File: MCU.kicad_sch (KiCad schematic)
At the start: 13 parts, among them U2201 ADG1607xCP, U2202 MSP430FR5969IRGZR, U2203 LP38690SDX-3.3/NOPB, U2204 TCAN4551RGYRQ1

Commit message: added second AMUX and housekeeping
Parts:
- added C1903: C_Small, Capacitor_SMD:C_0603_1608Metric_Pad1.08x0.95mm_HandSolder, symbol Device:C_Small
- added R1903: R_Small, Resistor_SMD:R_0603_1608Metric_Pad0.98x0.95mm_HandSolder, symbol Device:R_Small
- added TP1901, TP1902, TP1903, TP1904, TP1905, TP1906, TP1907, TP1908, TP1909, TP1910, TP1911: ~, symbol Connector:TestPoint_Small
- added U1902: ADG1607xCP, Package_CSP:LFCSP-32-1EP_5x5mm_P0.5mm_EP3.1x3.1mm, symbol Analog_Switch:ADG1607xCP
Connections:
- net AMEAS_BUS: now also U2201.21 (S5A); no longer U2202.7 (P3.3/A15/C15)
- net AMEAS_SOL_1: now also U1902.6 (S3B); no longer U2202.4 (P3.0/A12/C12)
- net AMEAS_SOL_2: now also U1902.5 (S4B); no longer U2202.5 (P3.1/A13/C13)
- net AMEAS_SOL_3: now also U1902.4 (S5B); no longer U2202.6 (P3.2/A14/C14)
- net AMUX_0: now also U1902.15 (A0)
- net AMUX_1: now also U1902.14 (A1)
- net AMUX_2: now also U1902.10 (A2)
- net AMUX_EN: now also U1902.16 (EN)
- net GND: now also C1903.1, R1903.1, U1902.25 (V_{SS}), U1902.33 (V_{SS}), U1902.9 (GND)
- net MCU_3V3: now also C1903.2, U1902.29 (V_{DD})
- net TMEAS_BATT_1: now also TP1910.1, U1902.19 (S3A); no longer U2202.39 (P2.3/TA0.0/UCA1STE/A6/C10)
- net TMEAS_BATT_2: now also TP1911.1, U1902.20 (S4A); no longer U2202.40 (P2.4/TA1.0/UCA1CLK/A7/C11)
- net TMEAS_SOL_1: now also TP1907.1
- net TMEAS_SOL_2: now also TP1908.1
- net TMEAS_SOL_3: now also TP1909.1
- net VMEAS_BATT_1: now also TP1905.1, U1902.17 (S1A); no longer U2202.3 (P1.2/TA1.1/TA0CLK/COUT/A2/C2)
- net VMEAS_BATT_2: now also TP1906.1, U1902.18 (S2A); no longer U2202.9 (P1.3/TA1.2/UCB0STE/A3/C3)
- net VMEAS_SOL_1: now also TP1902.1, U1902.21 (S5A); no longer U2202.16 (P4.0/A8)
- net VMEAS_SOL_2: now also TP1903.1, U1902.22 (S6A); no longer U2202.17 (P4.1/A9)
- net VMEAS_SOL_3: now also TP1904.1, U1902.23 (S7A); no longer U2202.18 (P4.2/A10)
- net at U2202.22 (TEST/SBWTCK): now also TP1901.1
- net at U2202.23 (~{RST}/NMI/SBWTDIO): now also R1903.2
- new net ADC_3: U1902.27 (DA), U2202.3 (P1.2/TA1.1/TA0CLK/COUT/A2/C2)
- new net ADC_4: U1902.31 (DB), U2202.9 (P1.3/TA1.2/UCB0STE/A3/C3)
- new net PWM_1: U2202.6 (P3.2/A14/C14)
- new net PWM_2: U2202.5 (P3.1/A13/C13)
- new net PWM_3: U2202.4 (P3.0/A12/C12)
- no-connect marks 1 -> 0
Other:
- moved on the sheet: C2201, U2201

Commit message: connected CAN driver, added 3 solar inputs
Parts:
- added C1904, C1905, C1906: C_Small, Capacitor_SMD:C_0603_1608Metric_Pad1.08x0.95mm_HandSolder, symbol Device:C_Small
- added R1904: R_Small, Resistor_SMD:R_0603_1608Metric_Pad0.98x0.95mm_HandSolder, symbol Device:R_Small
- added TP1912, TP1913, TP1914, TP1915, TP1916, TP1917, TP1918, TP1919: ~, symbol Connector:TestPoint_Small
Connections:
- net Ch_O_EN_11: now also TP1918.1
- net Ch_O_EN_12: now also TP1919.1
- net GND: now also U2204.20 (OSC2), C1904.1, C1905.1, C1906.1
- net MCU_3V3: now also U2204.15 (INH), U2204.17 (V_{IO}), C1904.2, R1904.1
- net TMEAS_BATT_1: now also U1902.8 (S1B); no longer U1902.19 (S3A)
- net TMEAS_BATT_2: now also U1902.7 (S2B); no longer U1902.20 (S4A)
- net VMEAS_SOL_1: now also U1902.19 (S3A); no longer U1902.21 (S5A)
- net VMEAS_SOL_2: now also U1902.20 (S4A); no longer U1902.22 (S6A)
- net VMEAS_SOL_3: now also U1902.21 (S5A); no longer U1902.23 (S7A)
- net PWM_4: now reaches U2202.16 (P4.0/A8)
- net PWM_5: now reaches U2202.17 (P4.1/A9)
- net PWM_6: now reaches U2202.18 (P4.2/A10)
- net CAN_~{INT}: now reaches U2202.19 (P4.3/A11)
- net CAN_~{INT}: now also U2204.8 (~{INT})
- net CAN_~{WKRQ}: now reaches U2202.33 (P4.4/TB0.5)
- net CAN_~{WKRQ}: now also U2204.2 (~{WKRQ})
- net CAN_CLK: now reaches U2202.39 (P2.3/TA0.0/UCA1STE/A6/C10)
- net CAN_CLK: now also U2204.1 (OSC1)
- net CAN_~{RST}: now reaches U2202.40 (P2.4/TA1.0/UCA1CLK/A7/C11)
- net CAN_~{RST}: now also U2204.19 (RST)
- net at U2204.12 (WAKE): now also R1904.2
- net at U2204.16 (V_{CCFLTR}): now also C1905.2
- net at U2204.18 (FLTR): now also C1906.2
- net AMEAS_SOL_6: now reaches U1902.1 (S8B)
- net AMEAS_SOL_5: now reaches U1902.2 (S7B)
- net VMEAS_SOL_6: now reaches U1902.24 (S8A)
- net VMEAS_SOL_6: now also TP1914.1
- net AMEAS_SOL_4: now reaches U1902.3 (S6B)
- new net TMEAS_SOL_4: TP1915.1
- new net TMEAS_SOL_5: TP1916.1
- new net TMEAS_SOL_6: TP1917.1
- new net VMEAS_SOL_4: TP1912.1, U1902.22 (S6A)
- new net VMEAS_SOL_5: TP1913.1, U1902.23 (S7A)
- no-connect marks 0 -> 3
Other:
- moved on the sheet: C2207, R2201, R2202, TP1902, TP1903, TP1904, TP1905, TP1906, TP1907, TP1908, TP1909, TP1910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

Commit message: changed IO epanders to 2nd MSP430
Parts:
- added C1908: C_Small, Capacitor_SMD:C_0603_1608Metric_Pad1.08x0.95mm_HandSolder, symbol Device:C_Small
- added R1910, R1911: R_Small, Resistor_SMD:R_0603_1608Metric_Pad0.98x0.95mm_HandSolder, symbol Device:R_Small
- added TP1920: ~, symbol Connector:TestPoint_Small
- added U1904: MSP430FR5969IRGZR, Package_DFN_QFN:Texas_RGZ0048A_VQFN-48-1EP_7x7mm_P0.5mm_EP5.15x5.15mm_ThermalVias, symbol MSP430FR5969IRGZR:MSP430FR5969IRGZR
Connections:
- net Ch_12V_EN_11: now also U1904.29 (P3.6/TB0.5)
- net Ch_12V_EN_12: now also U1904.21 (P2.6/TB0.1/UCA1RXD/UCA1SOM)
- net Ch_12V_EN_21: now also U1904.30 (P3.7/TB0.6)
- net Ch_12V_EN_22: now also U1904.38 (P2.7)
- net Ch_O_EN_11: now also U1904.4 (P3.0/A12/C12)
- net Ch_O_EN_12: now also U1904.24 (P2.0/TB0.6/UCA0TXD/UCA0SIMO/TB0CLK/ACLK)
- net Ch_O_EN_21: now also U1904.5 (P3.1/A13/C13)
- net Ch_O_EN_22: now also U1904.25 (P2.1/TB0.0/UCA0RXD/UCA0SOMI/TB0.0)
- net Ch_O_EN_31: now also U1904.6 (P3.2/A14/C14)
- net Ch_O_EN_32: now also U1904.26 (P2.2/TB0.2/UCB0CLK)
- net Ch_O_EN_41: now also U1904.7 (P3.3/A15/C15)
- net Ch_O_EN_42: now also U1904.39 (P2.3/TA0.0/UCA1STE/A6/C10)
- net Ch_O_EN_51: now also U1904.27 (P3.4/TB0.3/SMCLK)
- net Ch_O_EN_52: now also U1904.40 (P2.4/TA1.0/UCA1CLK/A7/C11)
- net Ch_O_EN_61: now also U1904.28 (P3.5/TB0.4/COUT)
- net Ch_O_EN_62: now also U1904.20 (P2.5/TB0.0/UCA1TXD/UCA1SIMO)
- net GND: now also C1908.1, R1911.1, U1904.36 (DVSS), U1904.41 (AVSS), U1904.44 (AVSS), U1904.47 (AVSS), U1904.49 (EXP), U1904.50 (EXP), U1904.51 (EXP), U1904.52 (EXP), U1904.53 (EXP), U1904.54 (EXP), U1904.55 (EXP), U1904.56 (EXP), U1904.57 (EXP), U1904.58 (EXP), U1904.59 (EXP), U1904.60 (EXP), U1904.61 (EXP)
- net MCU_3V3: now also R1910.2, U1904.37 (DVCC)
- net SCL: now also U1904.31 (P1.6/TB0.3/UCB0SIMO/UCB0SDA/TA0.0)
- net SDA: now also U1904.32 (P1.7/TB0.4/UCB0SOMI/UCB0SCL/TA1.0)
- net ~{GPIO_EX_RST}: no longer names the net of U2202.11 (P1.5/TB0.2/UCA0CLK/A5/C5)
- new net: R1911.2, U1904.23 (~{RST}/NMI/SBWTDIO)
- new net: C1908.2, R1910.1, U1904.48 (AVCC)
- new net: TP1920.1, U1904.22 (TEST/SBWTCK)
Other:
- removed sheet IO_Expander_1
- removed sheet IO_Expander_2
- added sheet RS422_485 (RS422_485.kicad_sch)
- moved on the sheet: C1903, C1904, C1905, C1906, C2201, C2202, C2203, C2204, C2205, C2206, C2207, R1903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

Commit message: added RS422, housekeeping
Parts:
- added R1901, R1902: R_Small, Resistor_SMD:R_0603_1608Metric_Pad0.98x0.95mm_HandSolder, symbol Device:R_Small
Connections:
- net MCU_3V3: now also R1901.2, R1902.2
- net SCL: now also R1902.1
- net SDA: now also R1901.1
- net SOL_TGGL_1: now also U1904.16 (P4.0/A8); no longer U2202.34 (P4.5)
- net SOL_TGGL_2: now also U1904.17 (P4.1/A9); no longer U2202.35 (P4.6)
- net SOL_TGGL_3: now also U1904.18 (P4.2/A10); no longer U2202.8 (P4.7)
- net RS_DE: now reaches U2202.11 (P1.5/TB0.2/UCA0CLK/A5/C5)
- net AMEAS_12V_1 renamed AMEAS_9
- net AMEAS_12V_2 renamed AMEAS_10
- net AMEAS_5V_1 renamed AMEAS_7
- net AMEAS_5V_2 renamed AMEAS_8
- net AMEAS_O_1 renamed AMEAS_1
- net AMEAS_O_2 renamed AMEAS_2
- net AMEAS_O_3 renamed AMEAS_3
- net AMEAS_O_4 renamed AMEAS_4
- net AMEAS_O_5 renamed AMEAS_5
- net AMEAS_O_6 renamed AMEAS_6
- net Ch_12V_EN_11 renamed Ch_EN_91
- net Ch_12V_EN_12 renamed Ch_EN_92
- net Ch_12V_EN_21 renamed Ch_EN_101
- net Ch_12V_EN_22 renamed Ch_EN_102
- net Ch_5V_EN_1 renamed Ch_EN_7x
- net Ch_5V_EN_2 renamed Ch_EN_8x
- net Ch_O_EN_11 renamed Ch_EN_11
- net Ch_O_EN_12 renamed Ch_EN_12
- net Ch_O_EN_21 renamed Ch_EN_21
- net Ch_O_EN_22 renamed Ch_EN_22
- net Ch_O_EN_31 renamed Ch_EN_31
- net Ch_O_EN_32 renamed Ch_EN_32
- net Ch_O_EN_41 renamed Ch_EN_41
- net Ch_O_EN_42 renamed Ch_EN_42
- net Ch_O_EN_51 renamed Ch_EN_51
- net Ch_O_EN_52 renamed Ch_EN_52
- net Ch_O_EN_61 renamed Ch_EN_61
- net Ch_O_EN_62 renamed Ch_EN_62
- net PWM_4: no longer names the net of U2202.16 (P4.0/A8)
- net PWM_5: no longer names the net of U2202.17 (P4.1/A9)
- net PWM_6: no longer names the net of U2202.18 (P4.2/A10)
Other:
- moved on the sheet: C1904, C1905, C1906, R1904, R2202, U2204

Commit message: updated battery pack module; updated solar inputs module
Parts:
- C1907: renamed from C2206; value 10u -> 100n
- renumbered C2202 to C1901, C2203 to C1902, C2201 to C1903, C1903 to C1904, C2204 to C1905, C2205 to C1906, C2207 to C1908, C1908 to C1909, C1904 to C1910, C1905 to C1911, C1906 to C1912, R1911 to R1904, R2201 to R1905, R1910 to R1906, R2202 to R1907, R1904 to R1908, TP1902 to TP1901, TP1903 to TP1902, TP1904 to TP1903, TP1912 to TP1904, TP1913 to TP1905, TP1914 to TP1906, TP1905 to TP1907, TP1906 to TP1908, TP1907 to TP1909, TP1908 to TP1910, TP1909 to TP1911, TP1915 to TP1912, TP1916 to TP1913, TP1917 to TP1914, TP1910 to TP1915, TP1911 to TP1916, TP1918 to TP1917, TP1919 to TP1918, TP1901 to TP1919, U2201 to U1901, U2203 to U1903, U2202 to U1904, U1904 to U1905, U2204 to U1906
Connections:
- net Ch_EN_7x: now also U1905.42 (PJ.6/HFXIN); no longer U1904.42 (PJ.6/HFXIN)
- net Ch_EN_8x: now also U1905.43 (PJ.7/HFXOUT); no longer U1904.43 (PJ.7/HFXOUT)
- net MCU_CHECK: now reaches U1904.10 (P1.4/TB0.1/UCA0STE/A4/C4)
- net MCU_CHECK: now also U1905.10 (P1.4/TB0.1/UCA0STE/A4/C4)
- net SOL_STAT_1: now reaches U1905.33 (P4.4/TB0.5)
- net SOL_STAT_2: now reaches U1905.34 (P4.5)
- net MPPT_~{EN}: now reaches U1905.8 (P4.7)
- net 5V_DCDC_MCU/VOUT renamed 5V_DCDC_1/VOUT
- net PWM_1: no longer names the net of U1904.6 (P3.2/A14/C14)
- net PWM_2: no longer names the net of U1904.5 (P3.1/A13/C13)
- net PWM_3: no longer names the net of U1904.4 (P3.0/A12/C12)
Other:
- removed sheet 5V_DCDC_MCU
- added sheet 5V_DCDC_1 (LDO_5V.kicad_sch)
- note added: "Both LOW = some MPPT in FAULT"
- note removed: "These are used for Radio ->direct connection to MCU"

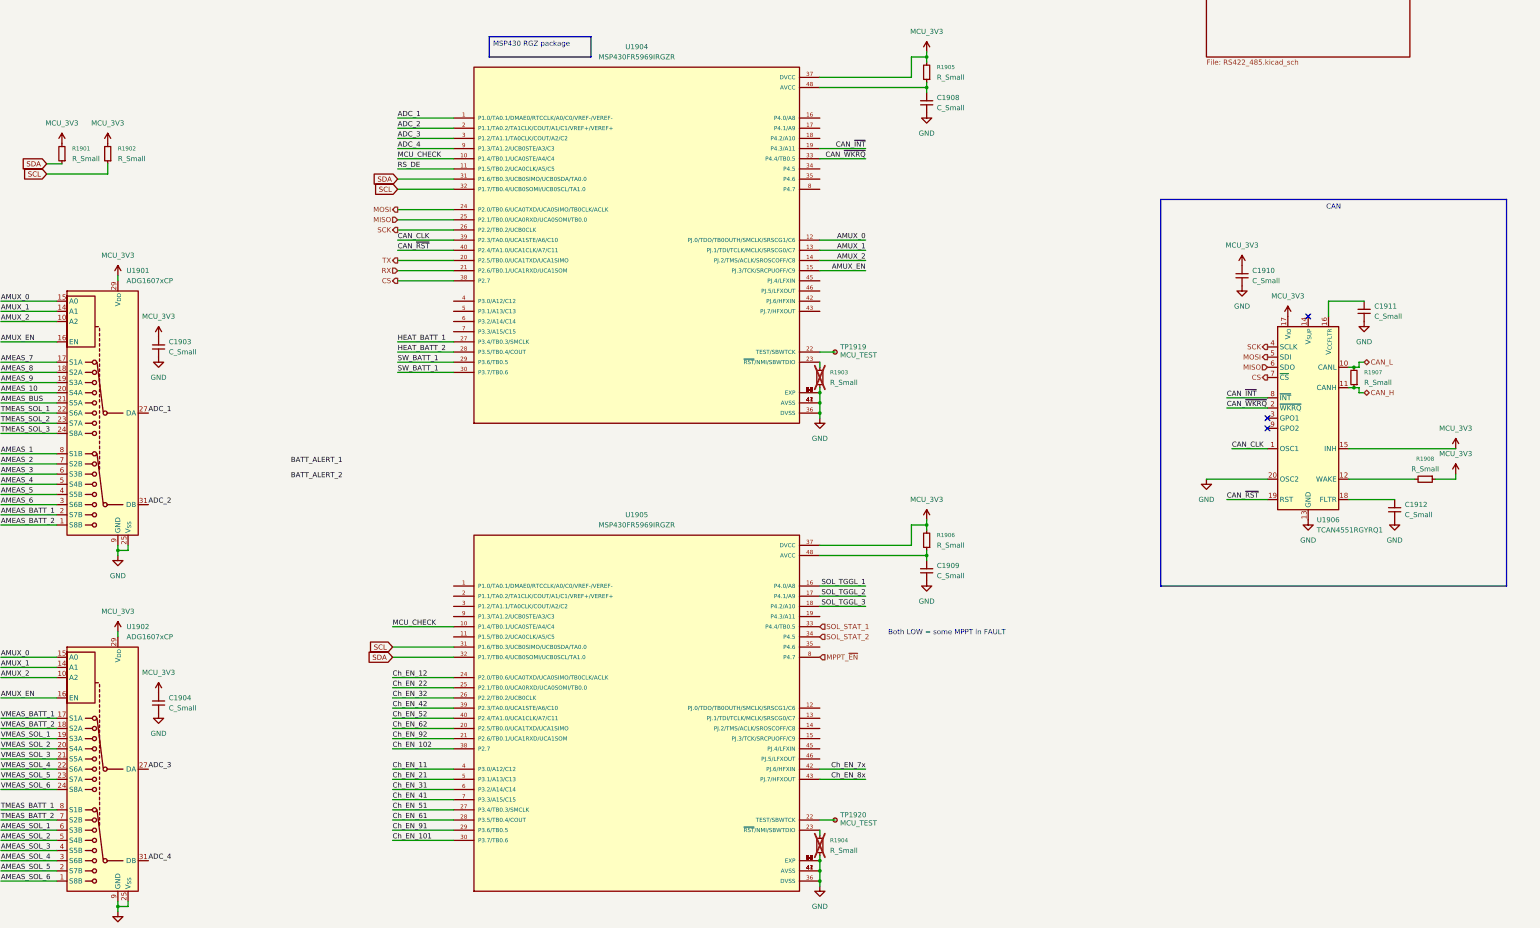
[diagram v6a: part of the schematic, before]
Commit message: added values to most parts
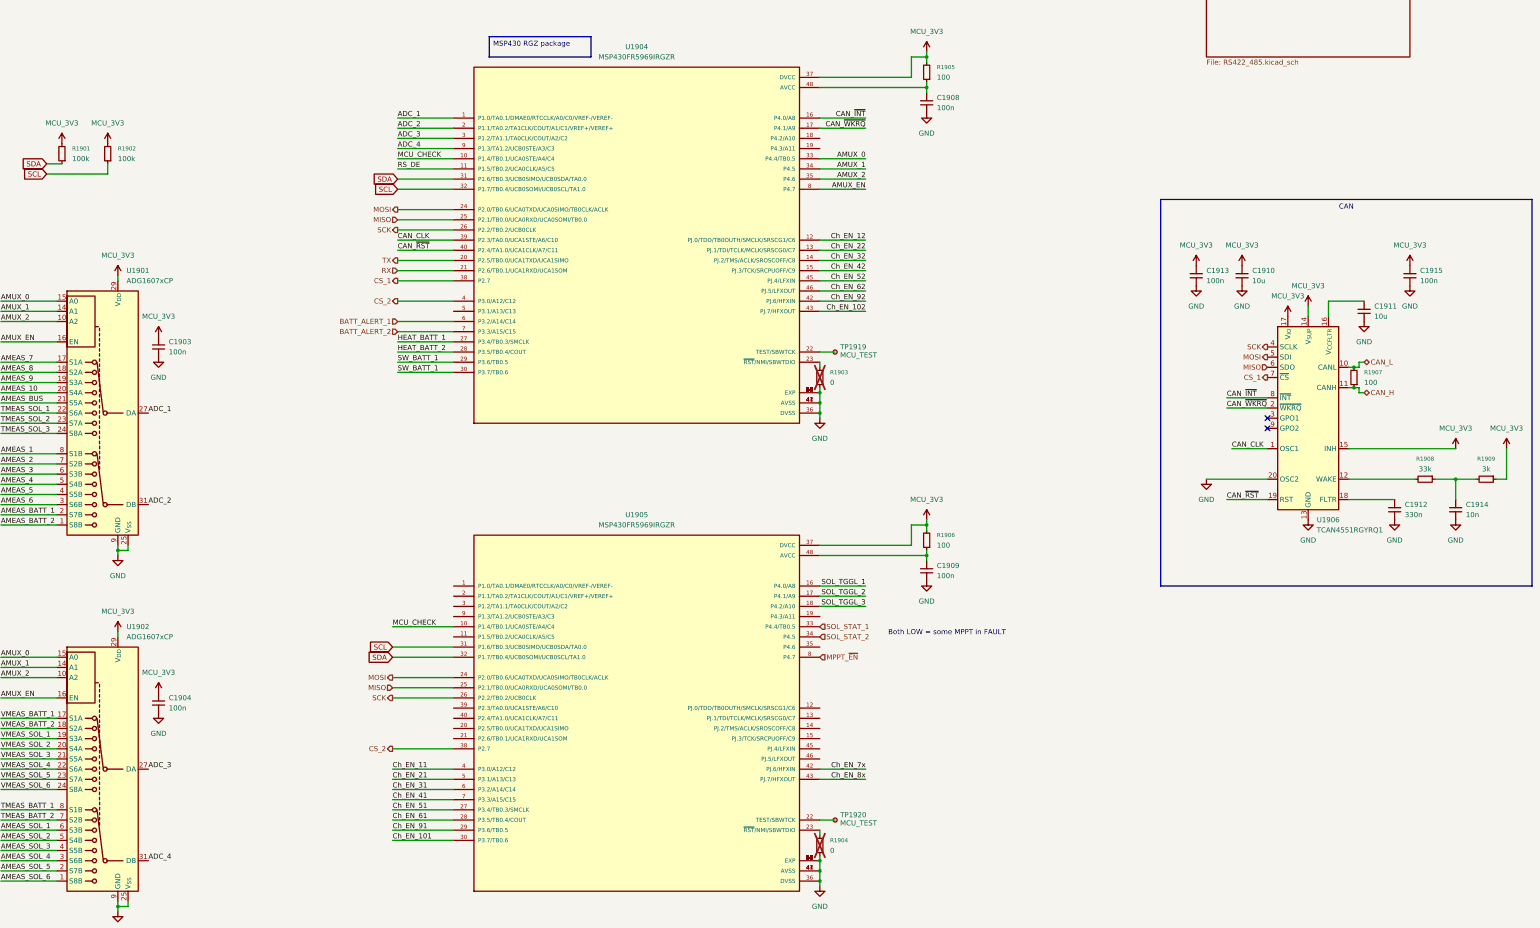
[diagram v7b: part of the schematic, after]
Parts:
- added C1913, C1915: 100n, Capacitor_SMD:C_0603_1608Metric_Pad1.08x0.95mm_HandSolder, symbol Device:C_Small
- added C1914: 10n, Capacitor_SMD:C_0603_1608Metric_Pad1.08x0.95mm_HandSolder, symbol Device:C_Small
- added R1909: 3k, Resistor_SMD:R_0603_1608Metric_Pad0.98x0.95mm_HandSolder, symbol Device:R_Small
- C1903, C1904, C1908, C1909: value C_Small -> 100n
- C1910, C1911: value C_Small -> 10u
- C1912: value C_Small -> 330n
- R1901, R1902: value R_Small -> 100k
- R1903, R1904: value R_Small -> 0
- R1905, R1906, R1907: value R_Small -> 100
- R1908: value R_Small -> 33k
- TP1901, TP1902, TP1903, TP1904, TP1905, TP1906, TP1907, TP1908, TP1909, TP1910, TP1911, TP1912, TP1913, TP1914, TP1915, TP1916, TP1917, TP1918, TP1919, TP1920: footprint (none) -> TestPoint:TestPoint_Pad_1.0x1.0mm
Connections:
- net AMUX_0: now also U1904.33 (P4.4/TB0.5); no longer U1904.12 (PJ.0/TDO/TB0OUTH/SMCLK/SRSCG1/C6)
- net AMUX_1: now also U1904.34 (P4.5); no longer U1904.13 (PJ.1/TDI/TCLK/MCLK/SRSCG0/C7)
- net AMUX_2: now also U1904.35 (P4.6); no longer U1904.14 (PJ.2/TMS/ACLK/SROSCOFF/C8)
- net AMUX_EN: now also U1904.8 (P4.7); no longer U1904.15 (PJ.3/TCK/SRCPUOFF/C9)
- net BATT_ALERT_1: now also U1904.6 (P3.2/A14/C14)
- net BATT_ALERT_2: now also U1904.7 (P3.3/A15/C15)
- net CAN_~{INT}: now also U1904.16 (P4.0/A8); no longer U1904.19 (P4.3/A11)
- net CAN_~{WKRQ}: now also U1904.17 (P4.1/A9); no longer U1904.33 (P4.4/TB0.5)
- net Ch_EN_102: now also U1904.43 (PJ.7/HFXOUT); no longer U1905.38 (P2.7)
- net Ch_EN_12: now also U1904.12 (PJ.0/TDO/TB0OUTH/SMCLK/SRSCG1/C6); no longer U1905.24 (P2.0/TB0.6/UCA0TXD/UCA0SIMO/TB0CLK/ACLK)
- net Ch_EN_22: now also U1904.13 (PJ.1/TDI/TCLK/MCLK/SRSCG0/C7); no longer U1905.25 (P2.1/TB0.0/UCA0RXD/UCA0SOMI/TB0.0)
- net Ch_EN_32: now also U1904.14 (PJ.2/TMS/ACLK/SROSCOFF/C8); no longer U1905.26 (P2.2/TB0.2/UCB0CLK)
- net Ch_EN_42: now also U1904.15 (PJ.3/TCK/SRCPUOFF/C9); no longer U1905.39 (P2.3/TA0.0/UCA1STE/A6/C10)
- net Ch_EN_52: now also U1904.45 (PJ.4/LFXIN); no longer U1905.40 (P2.4/TA1.0/UCA1CLK/A7/C11)
- net Ch_EN_62: now also U1904.46 (PJ.5/LFXOUT); no longer U1905.20 (P2.5/TB0.0/UCA1TXD/UCA1SIMO)
- net Ch_EN_92: now also U1904.42 (PJ.6/HFXIN); no longer U1905.21 (P2.6/TB0.1/UCA1RXD/UCA1SOM)
- net GND: now also C1913.1, C1914.1, C1915.1
- net MCU_3V3: now also U1906.14 (V_{SUP}), C1913.2, C1915.2, R1909.1; no longer R1908.1
- net MISO: now also U1905.25 (P2.1/TB0.0/UCA0RXD/UCA0SOMI/TB0.0)
- net MOSI: now also U1905.24 (P2.0/TB0.6/UCA0TXD/UCA0SIMO/TB0CLK/ACLK)
- net SCK: now also U1905.26 (P2.2/TB0.2/UCB0CLK)
- net CS_2: now reaches U1904.4 (P3.0/A12/C12)
- net CS_2: now also U1905.38 (P2.7)
- net CS renamed CS_1
- new net: C1914.2, R1908.1, R1909.2
- no-connect marks 3 -> 2
